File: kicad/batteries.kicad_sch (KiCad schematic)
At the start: 11 parts, among them J1 ActivEnergy B2+, J2 ActivEnergy B1+, J3 Makita Plus, J4 Makita Plus, J5 Makita Minus, J6 Makita Minus, J7 ActivEnergy B2-, J8 ActivEnergy B1-

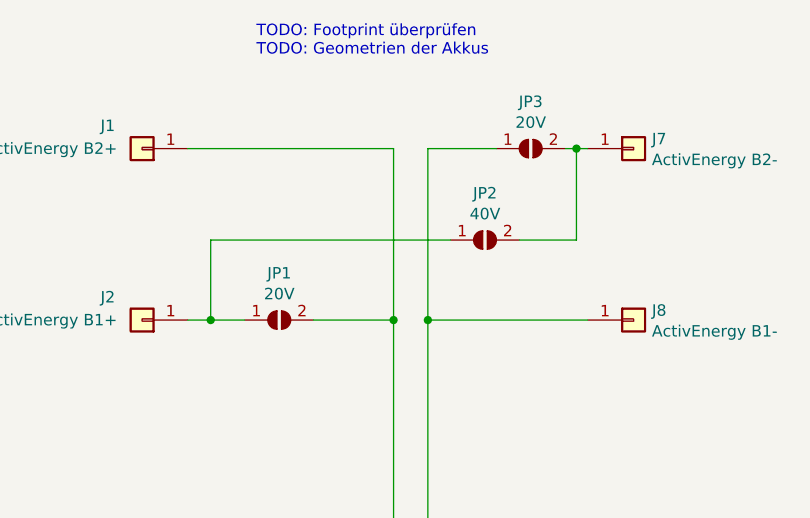
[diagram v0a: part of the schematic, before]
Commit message: created bom for order lcsc
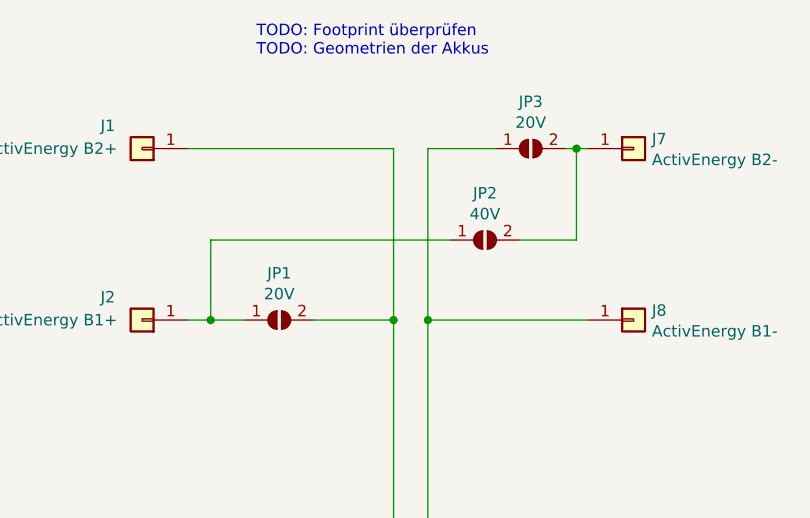
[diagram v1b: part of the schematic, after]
